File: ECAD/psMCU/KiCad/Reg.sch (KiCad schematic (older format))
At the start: 17 parts, among them U258 SN74LVC1G04DCK, U259 CD74HC173PW, U260 CD74HC173PW, U261 SN74LVC1G126DCK, U262 SN74LVC1G04DCK, U263 SN74HC245PW

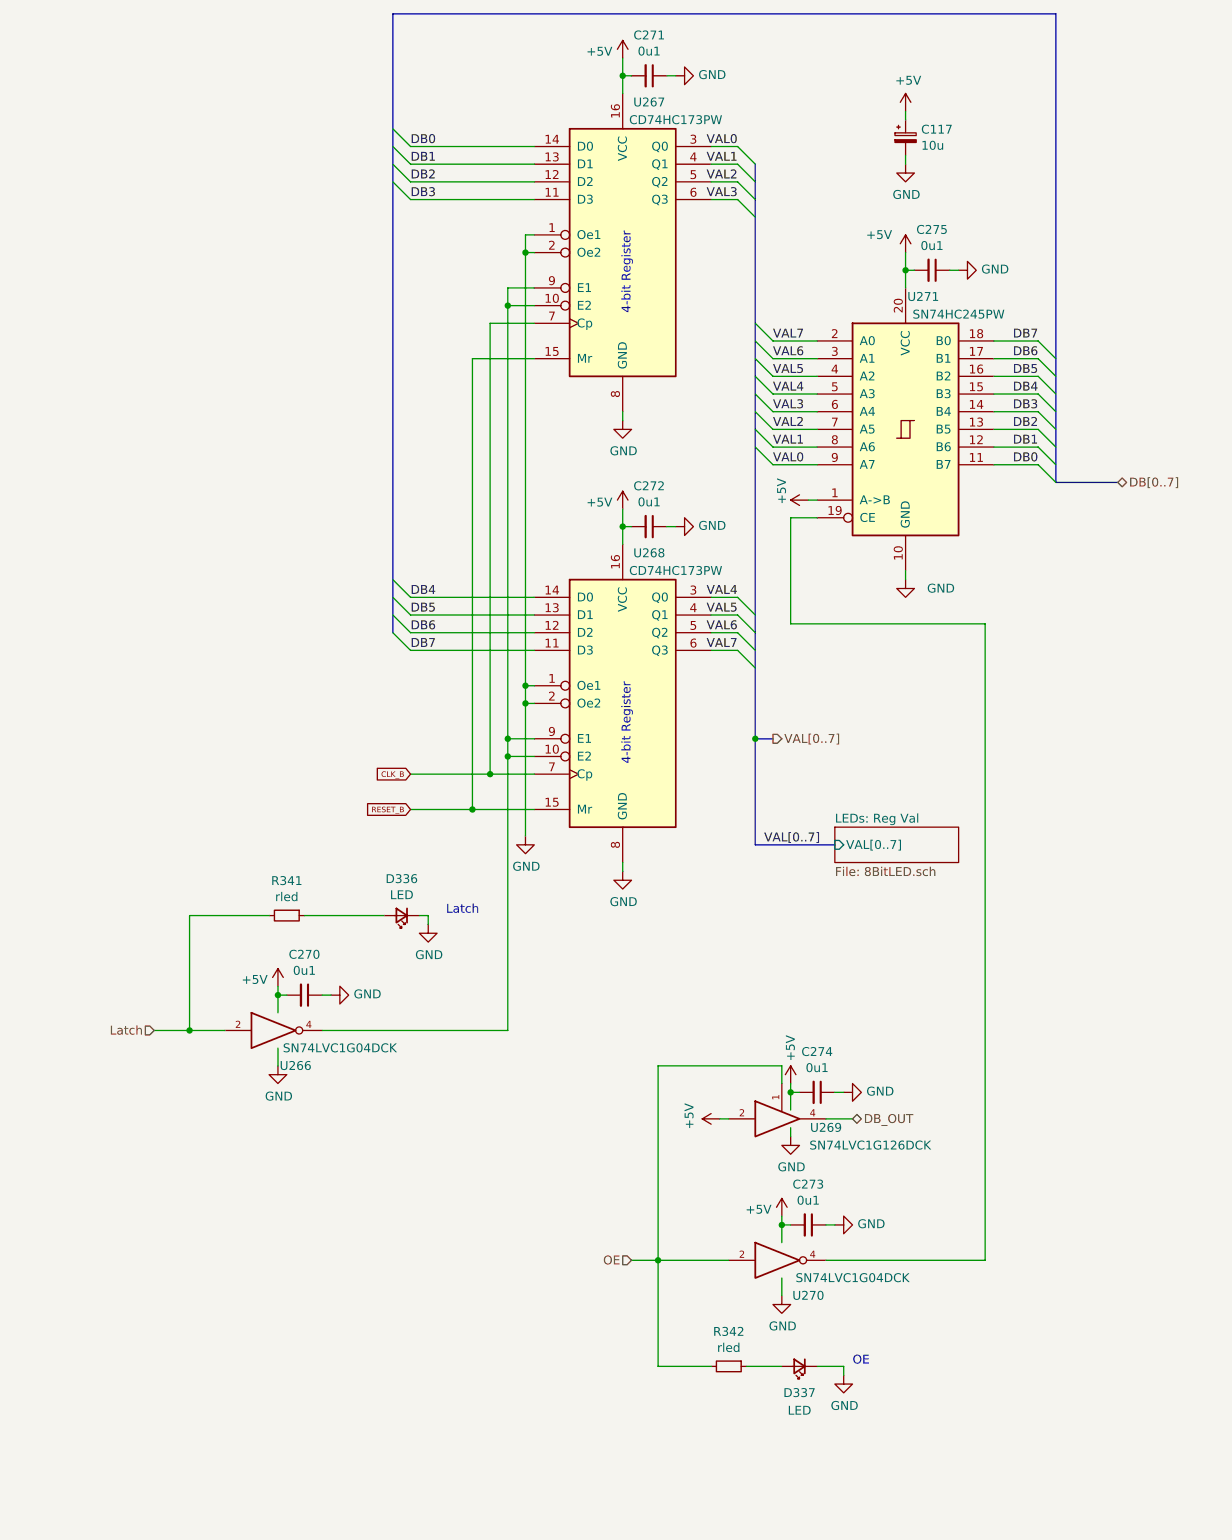
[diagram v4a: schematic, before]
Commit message: Sch: Implemented much improved debugger interface
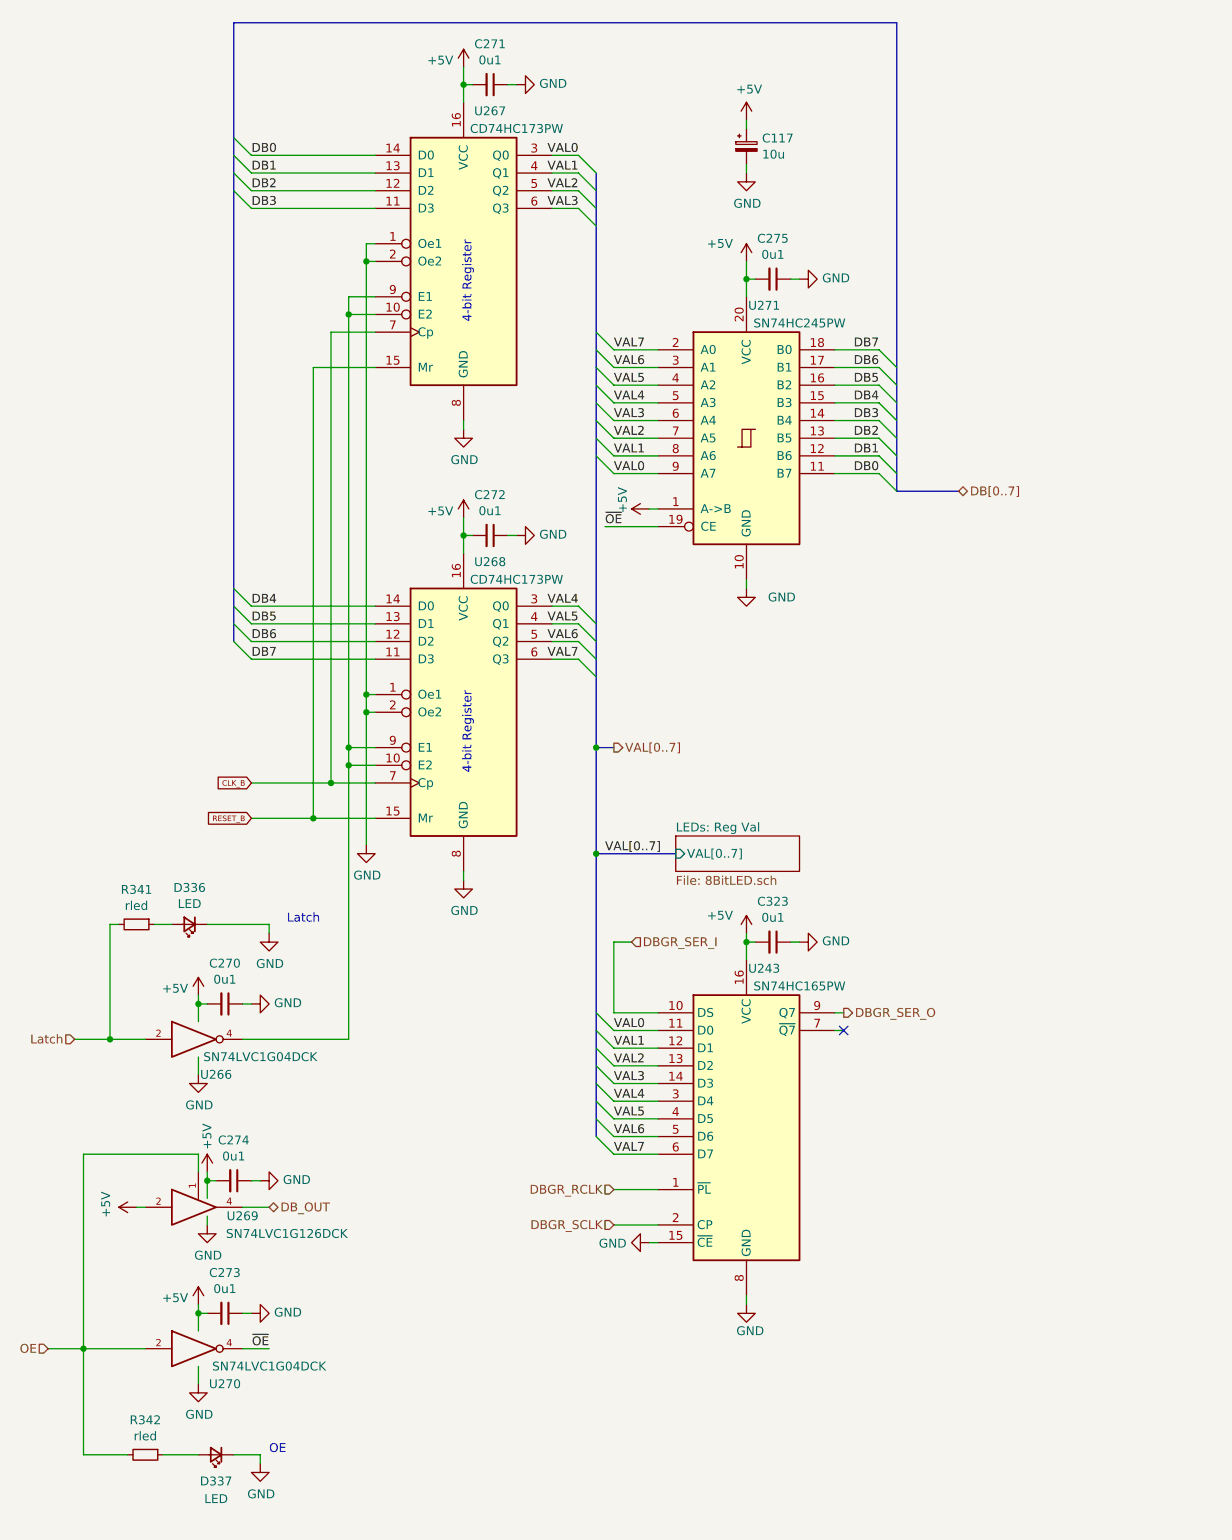
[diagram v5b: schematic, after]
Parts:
- added C322: 0u1, NoRef_Footprints:C_0603_1608Metric_NoRef, symbol Device:C_Small
- added U242: SN74HC165PW, Package_SO:TSSOP-16_4.4x5mm_P0.65mm, symbol 74xx:74LS165
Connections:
- net +5V: now also C322.2, U242.16 (VCC)
- net GND: now also C322.1, U242.15 (~CE), U242.8 (GND)
- net VAL0: now also U242.11 (D0)
- net VAL1: now also U242.12 (D1)
- net VAL2: now also U242.13 (D2)
- net VAL3: now also U242.14 (D3)
- net VAL4: now also U242.3 (D4)
- net VAL5: now also U242.4 (D5)
- net VAL6: now also U242.5 (D6)
- net VAL7: now also U242.6 (D7)
- net ~OE: now reaches U262.4, U263.19 (CE)
- new net DBGR_RCLK: U242.1 (~PL)
- new net DBGR_SCLK: U242.2 (CP)
- new net DBGR_SER_I: U242.10 (DS)
- new net DBGR_SER_O: U242.9 (Q7)
- no-connect marks 0 -> 1
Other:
- moved on the sheet: C117, C270, C271, C272, C273, C274, C275, D336, D337, R341, R342, U266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

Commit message: Sch: Addded Buffer for external interrupt assert
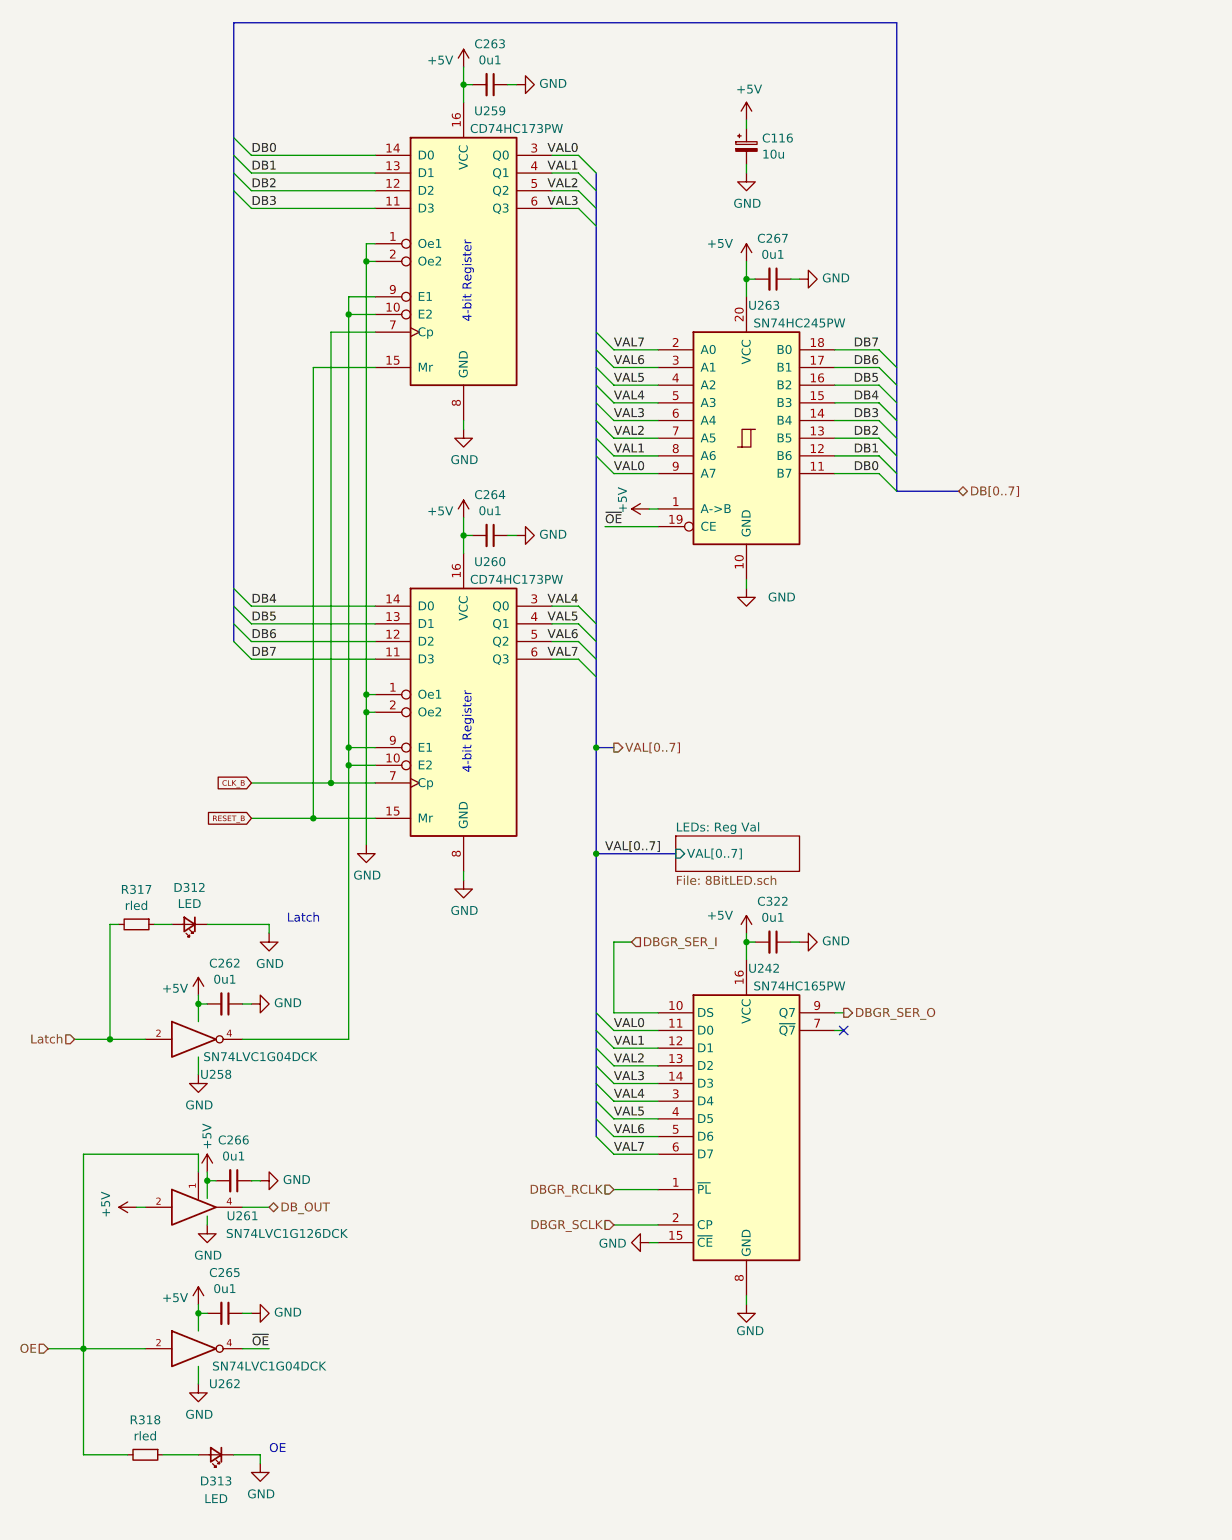
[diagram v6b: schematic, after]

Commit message: Sch: Modified instruction set to add fast memory access functions.
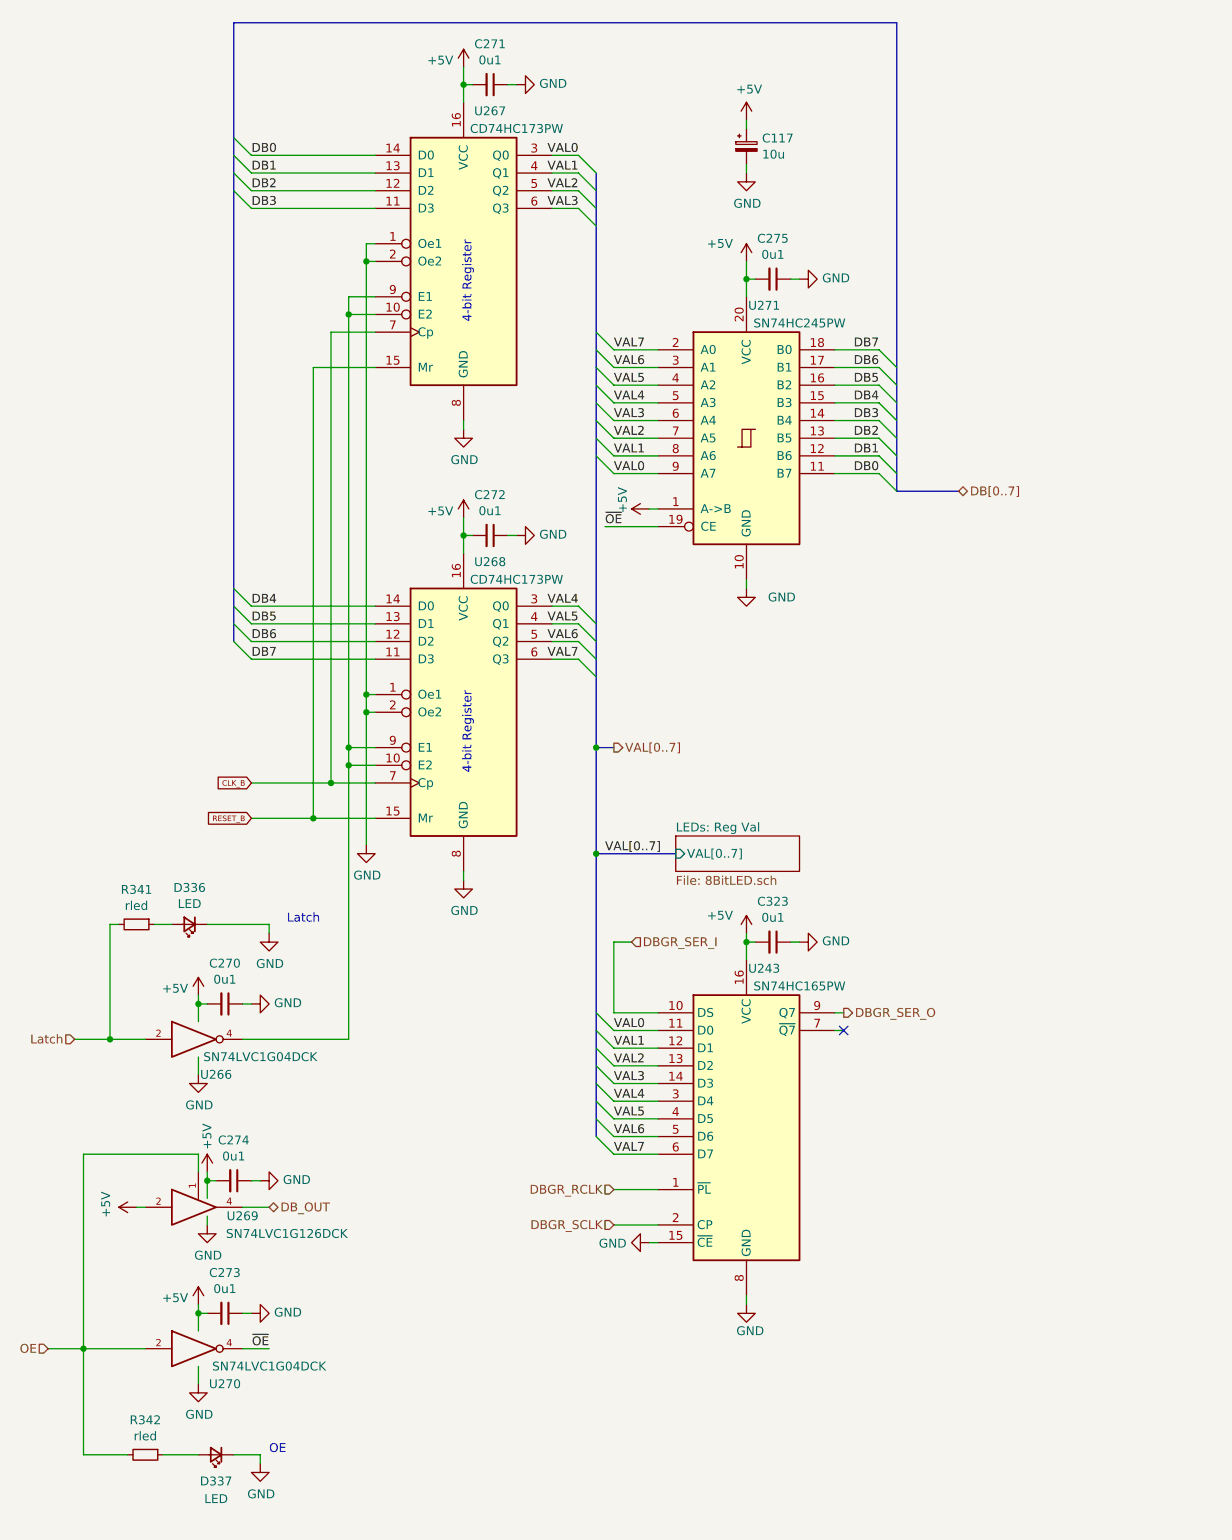
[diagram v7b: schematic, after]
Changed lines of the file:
@@
 $Descr A4 8268 11693 portrait
 encoding utf-8
-Sheet 51 105
+Sheet 24 109
 Title "psMCU"
 Date "2022-02-13"
@@
 AR Path="/61C3CF7F/5F0B921F" Ref="U262"  Part="1"
 AR Path="/61C3CF88/5F0B921F" Ref="U270"  Part="1"
-F 0 "U262" H 1650 8400 50  0000 C CNN
+F 0 "U270" H 1650 8400 50  0000 C CNN
 F 1 "SN74LVC1G04DCK" H 1900 8500 50  0000 C CNN
 F 2 "Package_TO_SOT_SMD:SOT-353_SC-70-5" H 1500 8600 50  0001 C CNN
@@
 AR Path="/61C3CF7F/5F0B922C" Ref="C265"  Part="1"
 AR Path="/61C3CF88/5F0B922C" Ref="C273"  Part="1"
-F 0 "C265" V 1421 8400 50  0000 C CNN
+F 0 "C273" V 1421 8400 50  0000 C CNN
 F 1 "0u1" V 1512 8400 50  0000 C CNN
 F 2 "NoRef_Footprints:C_0603_1608Metric_NoRef" H 1650 8400 50  0001 C CNN
@@
 AR Path="/61C3CF7F/5EF8C8C3" Ref="C262"  Part="1"
 AR Path="/61C3CF88/5EF8C8C3" Ref="C270"  Part="1"
-F 0 "C262" V 1421 6650 50  0000 C CNN
+F 0 "C270" V 1421 6650 50  0000 C CNN
 F 1 "0u1" V 1512 6650 50  0000 C CNN
 F 2 "NoRef_Footprints:C_0603_1608Metric_NoRef" H 1650 6650 50  0001 C CNN
@@
 AR Path="/61C3CF7F/5EF829AC" Ref="U258"  Part="1"
 AR Path="/61C3CF88/5EF829AC" Ref="U266"  Part="1"
-F 0 "U258" H 1600 6650 50  0000 C CNN
+F 0 "U266" H 1600 6650 50  0000 C CNN
 F 1 "SN74LVC1G04DCK" H 1850 6750 50  0000 C CNN
 F 2 "Package_TO_SOT_SMD:SOT-353_SC-70-5" H 1500 6850 50  0001 C CNN
@@
 AR Path="/61C3CF7F/5ED710F5" Ref="C267"  Part="1"
 AR Path="/61C3CF88/5ED710F5" Ref="C275"  Part="1"
-F 0 "C267" V 4521 2550 50  0000 C CNN
+F 0 "C275" V 4521 2550 50  0000 C CNN
 F 1 "0u1" V 4612 2550 50  0000 C CNN
 F 2 "NoRef_Footprints:C_0603_1608Metric_NoRef" H 4750 2550 50  0001 C CNN
@@
 AR Path="/61C3CF7F/5ED33B48" Ref="C264"  Part="1"
 AR Path="/61C3CF88/5ED33B48" Ref="C272"  Part="1"
-F 0 "C264" V 2921 4000 50  0000 C CNN
+F 0 "C272" V 2921 4000 50  0000 C CNN
 F 1 "0u1" V 3012 4000 50  0000 C CNN
 F 2 "NoRef_Footprints:C_0603_1608Metric_NoRef" H 3150 4000 50  0001 C CNN
@@
 AR Path="/61C3CF7F/5ED33B3B" Ref="U260"  Part="1"
 AR Path="/61C3CF88/5ED33B3B" Ref="U268"  Part="1"
-F 0 "U260" H 3150 5850 50  0000 C CNN
+F 0 "U268" H 3150 5850 50  0000 C CNN
 F 1 "CD74HC173PW" H 3300 5750 50  0000 C CNN
 F 2 "Package_SO:TSSOP-16_4.4x5mm_P0.65mm" H 3000 5000 50  0001 C CNN
@@
 AR Path="/61C3CF7F/5ED2F1C3" Ref="C263"  Part="1"
 AR Path="/61C3CF88/5ED2F1C3" Ref="C271"  Part="1"
-F 0 "C263" V 2921 1450 50  0000 C CNN
+F 0 "C271" V 2921 1450 50  0000 C CNN
 F 1 "0u1" V 3012 1450 50  0000 C CNN
 F 2 "NoRef_Footprints:C_0603_1608Metric_NoRef" H 3150 1450 50  0001 C CNN
@@
 AR Path="/61C3CF7F/5ED2BCE4" Ref="U259"  Part="1"
 AR Path="/61C3CF88/5ED2BCE4" Ref="U267"  Part="1"
-F 0 "U259" H 3150 3300 50  0000 C CNN
+F 0 "U267" H 3150 3300 50  0000 C CNN
 F 1 "CD74HC173PW" H 3300 3200 50  0000 C CNN
 F 2 "Package_SO:TSSOP-16_4.4x5mm_P0.65mm" H 3000 2450 50  0001 C CNN
@@
 AR Path="/61C3CF7F/5F369738" Ref="C266"  Part="1"
 AR Path="/61C3CF88/5F369738" Ref="C274"  Part="1"
-F 0 "C266" V 1471 7650 50  0000 C CNN
+F 0 "C274" V 1471 7650 50  0000 C CNN
 F 1 "0u1" V 1562 7650 50  0000 C CNN
 F 2 "NoRef_Footprints:C_0603_1608Metric_NoRef" H 1700 7650 50  0001 C CNN
@@
 AR Path="/61C3CF7F/62B8F34C" Ref="D313"  Part="1"
 AR Path="/61C3CF88/62B8F34C" Ref="D337"  Part="1"
-F 0 "D313" H 1600 9350 50  0000 C CNN
+F 0 "D337" H 1600 9350 50  0000 C CNN
 F 1 "LED" H 1600 9450 50  0000 C CNN
 F 2 "NoRef_Footprints:D_0603_1608Metric_NoRef" V 1600 9200 50  0001 C CNN
@@
 AR Path="/61C3CF7F/62B8F35A" Ref="R318"  Part="1"
 AR Path="/61C3CF88/62B8F35A" Ref="R342"  Part="1"
-F 0 "R318" V 1004 9200 50  0000 C CNN
+F 0 "R342" V 1004 9200 50  0000 C CNN
 F 1 "rled" V 1095 9200 50  0000 C CNN
 F 2 "NoRef_Footprints:R_0603_1608Metric_NoRef" H 1200 9200 50  0001 C CNN
@@
 AR Path="/61C3CF7F/62B948BD" Ref="D312"  Part="1"
 AR Path="/61C3CF88/62B948BD" Ref="D336"  Part="1"
-F 0 "D312" H 1450 5993 50  0000 C CNN
+F 0 "D336" H 1450 5993 50  0000 C CNN
 F 1 "LED" H 1450 6084 50  0000 C CNN
 F 2 "NoRef_Footprints:D_0603_1608Metric_NoRef" V 1450 6200 50  0001 C CNN
@@
 AR Path="/61C3CF7F/62B948CB" Ref="R317"  Part="1"
 AR Path="/61C3CF88/62B948CB" Ref="R341"  Part="1"
-F 0 "R317" V 954 6200 50  0000 C CNN
+F 0 "R341" V 954 6200 50  0000 C CNN
 F 1 "rled" V 1045 6200 50  0000 C CNN
 F 2 "NoRef_Footprints:R_0603_1608Metric_NoRef" H 1150 6200 50  0001 C CNN
@@
 AR Path="/61C3CF7F/5F369721" Ref="U261"  Part="1"
 AR Path="/61C3CF88/5F369721" Ref="U269"  Part="1"
-F 0 "U261" H 1750 7750 50  0000 C CNN
+F 0 "U269" H 1750 7750 50  0000 C CNN
 F 1 "SN74LVC1G126DCK" H 2000 7650 50  0000 C CNN
 F 2 "Package_TO_SOT_SMD:SOT-353_SC-70-5" H 1500 7800 50  0001 C CNN
@@
 AR Path="/61C3CF88/6244A237" Ref="C117"  Part="1"
 AR Path="/61C3CF7F/6244A237" Ref="C116"  Part="1"
-F 0 "C116" H 4688 1846 50  0000 L CNN
+F 0 "C117" H 4688 1846 50  0000 L CNN
 F 1 "10u" H 4688 1755 50  0000 L CNN
 F 2 "" H 4600 1800 50  0001 C CNN
@@
 AR Path="/61C3CF7F/5ED4E5FA" Ref="U263"  Part="1"
 AR Path="/61C3CF88/5ED4E5FA" Ref="U271"  Part="1"
-F 0 "U263" H 4700 4200 50  0000 C CNN
+F 0 "U271" H 4700 4200 50  0000 C CNN
 F 1 "SN74HC245PW" H 4900 4100 50  0000 C CNN
 F 2 "Package_SO:TSSOP-20_4.4x6.5mm_P0.65mm" H 4600 3450 50  0001 C CNN
@@
 AR Path="/61C3CF7F/6474C9BF" Ref="C322"  Part="1"
 AR Path="/61C3CF88/6474C9BF" Ref="C323"  Part="1"
-F 0 "C322" V 4521 6300 50  0000 C CNN
+F 0 "C323" V 4521 6300 50  0000 C CNN
 F 1 "0u1" V 4612 6300 50  0000 C CNN
 F 2 "NoRef_Footprints:C_0603_1608Metric_NoRef" H 4750 6300 50  0001 C CNN
@@
 AR Path="/61C3CF7F/6474C9B9" Ref="U242"  Part="1"
 AR Path="/61C3CF88/6474C9B9" Ref="U243"  Part="1"
-F 0 "U242" H 4700 8150 50  0000 C CNN
+F 0 "U243" H 4700 8150 50  0000 C CNN
 F 1 "SN74HC165PW" H 4900 8050 50  0000 C CNN
 F 2 "Package_SO:TSSOP-16_4.4x5mm_P0.65mm" H 4600 7300 50  0001 C CNN

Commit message: Sch: Cleanup + Small fixes
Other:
- note added: "Debugger Input"
- moved on the sheet: C116, C262, C263, C264, C265, C266, C267, C322, D312, D313, R317, R318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
